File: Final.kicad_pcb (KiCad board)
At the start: 4 copper layers, 130 x 152.8 mm, 163 parts, among them J1 Power from Back_Board, J10 Conn_01x08_Socket, J11 GH-S37D, J12 LoadCell, J13 LoadCell, J14 Power to Main_Board, J15 ST-Link, J16 to TopBoard, J17 USB_C_Receptacle_USB2.0_16P, J18 LIDAR, J19 to Main_Board, J2 UnitV01, J20 to LED, J3 to LED, J4 to Tile_Board, J5 to LiDAR_Board, J6 ST-Link, J7 ST-Link, J8 UnitV02, J9 GH-S37D, M1 STS3032, M2 STS3032, M3 STS3032, M4 STS3032, SW1 RESET_SWITCH, SW10 TC-06104-043E, SW2 RESET_SWITCH, SW3 MODE_SWITCH, SW4 MODE_SWITCH, SW5 B-12CCP, SW6 B-12CCP, SW7 RESET_SWITCH, SW8 MODE_SWITCH, SW9 TC-06104-043E, U1 LT1085CM-3.3#PBF, U10 NJU77551F, U11 XIAO ESP32C3, U12 XIAO-RP2040-DIP, U13 RT9080-33GJ5, U14 CH340E, U15 STM32F446RET6, U16 AE-BNO055-BO, U17 S11059, U2 STM32F446RET6, U3 BNO085, U4 AE-BNO055-BO, U5 STM32H723ZGT6, U8 NJU77551F, U9 MAX3485

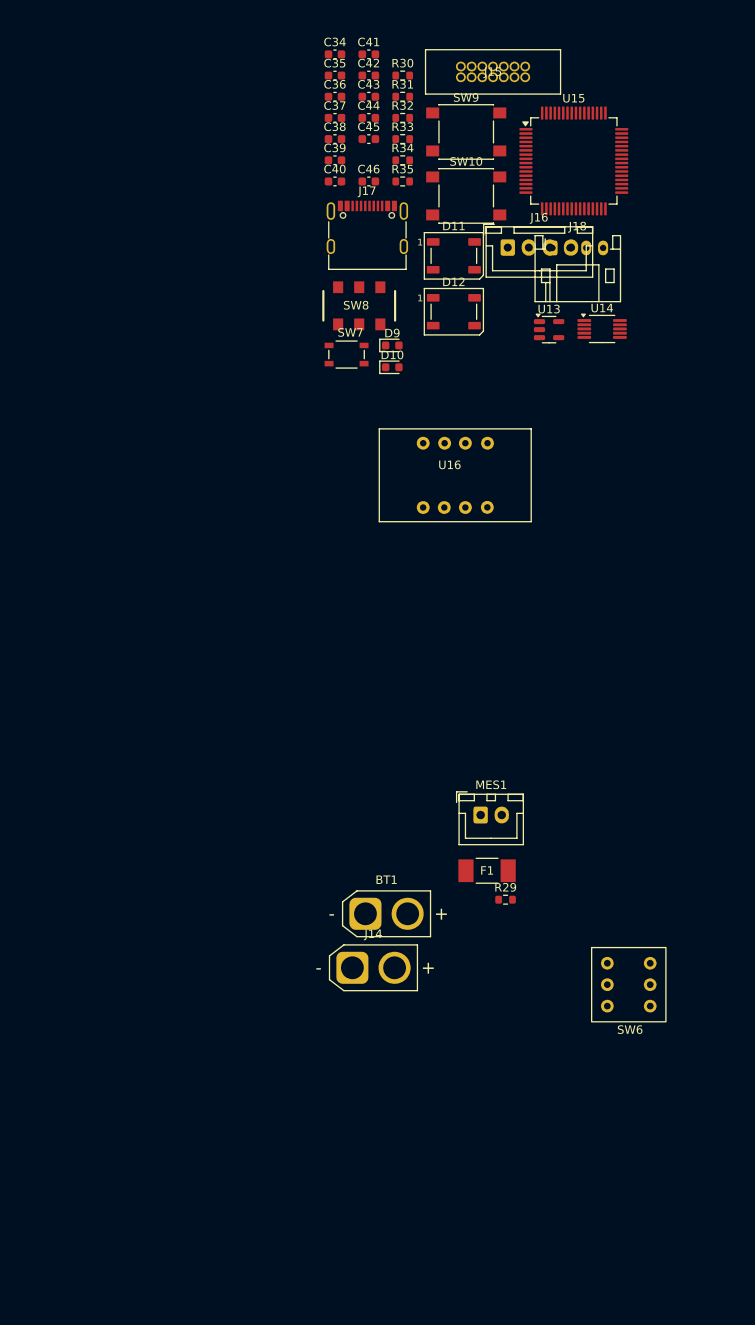
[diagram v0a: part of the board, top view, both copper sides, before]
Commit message: LiDAR基板Rev.3コネクタ配置
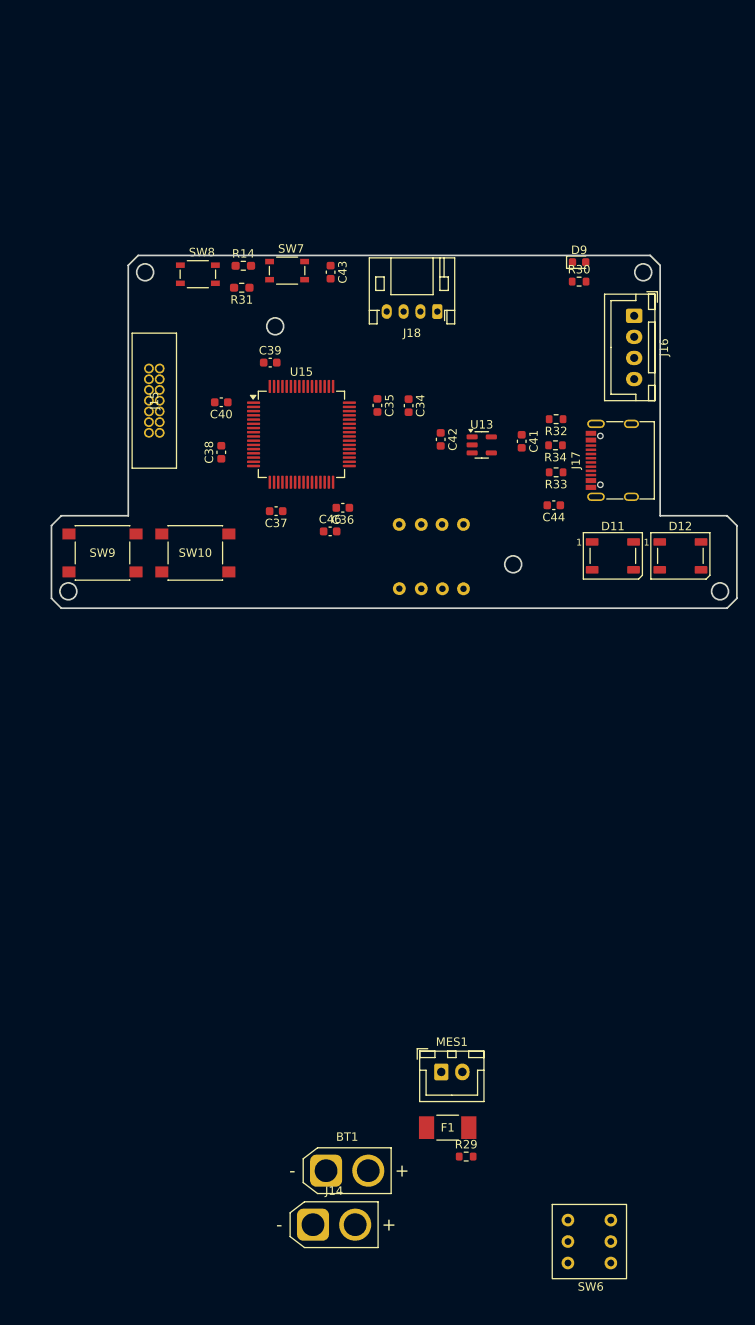
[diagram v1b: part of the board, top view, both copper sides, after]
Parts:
- removed C45: 0.1uF, Capacitor_SMD:C_0603_1608Metric
- removed D10: LED, LED_SMD:LED_0603_1608Metric
- removed R35: 470, Resistor_SMD:R_0603_1608Metric
- removed U14: CH340E, Package_SO:MSOP-10_3x3mm_P0.5mm
- added R14: 1k, Resistor_SMD:R_0603_1608Metric_Pad0.98x0.95mm_HandSolder, F.Cu at (212.8, 47.7)
- C44: value 0.1uF -> 4.7uF
- R30: value 470 -> 1k
- R31: footprint Resistor_SMD:R_0603_1608Metric -> Resistor_SMD:R_0603_1608Metric_Pad0.98x0.95mm_HandSolder
- R32: value 10k -> 1M
- R6, R8: value 10k -> 1k
- SW8: footprint SSSS213202:SSSS213202 -> SKRPACE010:SW_SKRPACE010
- U16: moved to B.Cu
- moved SW9 65.9 mm to (196.1, 81.7)
- moved J15 55.9 mm to (202.2, 63.7), turned to 90 degrees
- moved SW10 53.1 mm to (207.1, 81.7)
- moved C44 50.9 mm to (249.6, 76.0), turned to 180 degrees
- moved C41 49.3 mm to (245.8, 68.5), turned to -90 degrees
- moved C36 48.7 mm to (224.6, 76.3), turned to 180 degrees
- moved C37 47.1 mm to (216.7, 76.8), turned to 180 degrees
- moved U15 45.7 mm to (219.7, 67.7)
- moved C42 43.9 mm to (236.2, 68.2), turned to -90 degrees
- moved R33 43.5 mm to (249.8, 72.2), turned to 180 degrees
- moved C34 42.5 mm to (232.4, 64.2), turned to -90 degrees
- moved C46 41.7 mm to (223.1, 79.2)
- moved D11 40.2 mm to (256.6, 82.0)
- moved J17 40.1 mm to (257.7, 70.7), turned to 90 degrees
- moved R32 40.1 mm to (249.8, 65.8), turned to 180 degrees
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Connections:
- C44 pad 1: +5V -> Earth
- J17 pad A6: Net-(U14-UD+) -> unconnected-(J17-D+-PadA6)
- J17 pad A7: Net-(U14-UD-) -> unconnected-(J17-D--PadA7)
- J17 pad B6: Net-(U14-UD+) -> unconnected-(J17-D+-PadB6)
- J17 pad B7: Net-(U14-UD-) -> unconnected-(J17-D--PadB7)
- J17 pad S1: unconnected-(J17-SHIELD-PadS1)_2 -> Earth
- R31 pad 1: +3.3V -> GND
- R31 pad 2: Net-(SW8A-A) -> Net-(U15-BOOT0)
- R32 pad 1: GND -> Earth
- R32 pad 2: Net-(SW8A-C) -> GND
- SW8 pad 1: Net-(SW8A-A) -> Net-(R14-Pad2)
- SW8 pad 2: Net-(SW8A-B) -> Net-(U15-BOOT0)
- U15 pad 14: /LiDAR_Board/TX4 -> unconnected-(U15-PA0-Pad14)
- U15 pad 15: /LiDAR_Board/RX4 -> unconnected-(U15-PA1-Pad15)
- U15 pad 60: Net-(SW8A-B) -> Net-(U15-BOOT0)
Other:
- board size 130 x 152.8 mm -> 253.4 x 152.8 mm

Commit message: メイン基板Rev.3
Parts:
- removed BT1: Battery, Connector_AMASS:AMASS_XT30U-M_1x02_P5.0mm_Vertical
- removed F1: 0451015.MRL, 0451015.MRL:0451Series_LTF
- removed the J14 at (221.0, 161.3)
- removed MES1: Voltmeter_DC, Connector_JST:JST_XH_B2B-XH-A_1x02_P2.50mm_Vertical
- removed the R29 at (239.2, 153.2)
- removed SW10, SW9: TC-06104-043E, Button_Switch_SMD:SW_Push_1P1T_NO_6x6mm_H9.5mm
- removed SW6: B-12CCP, B-12CCP:B-12CCP
- added D12: WS2812B, LED_SMD:LED_WS2812B_PLCC4_5.0x5.0mm_P3.2mm, F.Cu at (203.7, 74.5)
- added D13: WS2812B, LED_SMD:LED_WS2812B_PLCC4_5.0x5.0mm_P3.2mm, F.Cu at (261.9, 85.3)
- added G***: LOGO, icon:jlcpcb-logo-pcb15-8, F.Cu at (243.5, 51.4)
- added G***: LOGO, icon:fornax-logo-pcb15-3.8, F.Cu at (243.6, 48.2)
- added G***: LOGO, icon:fornax-logo-pcb15-3.8, F.Cu at (232.8, 160.6)
- added IC1: R3111N211A-TR-FE, R3111N211A:SOT95P280X130-5N, F.Cu at (106.7, 47.9)
- added IC2: R3111N211A-TR-FE, R3111N211A:SOT95P280X130-5N, F.Cu at (79.2, 81.7)
- added R37: 5.6k, Resistor_SMD:R_0402_1005Metric, F.Cu at (101.2, 47.9)
- added R38: 2.4k, Resistor_SMD:R_0402_1005Metric, F.Cu at (103.5, 48.4)
- added R39: 470k, Resistor_SMD:R_0402_1005Metric, F.Cu at (106.0, 45.1)
- added R40: 5.6k, Resistor_SMD:R_0402_1005Metric, F.Cu at (74.6, 81.2)
- added R41: 470k, Resistor_SMD:R_0402_1005Metric, F.Cu at (78.5, 79.0)
- added R42: 2.4k, Resistor_SMD:R_0402_1005Metric, F.Cu at (76.1, 82.2)
- C51: renamed from C43; footprint Capacitor_SMD:C_0603_1608Metric -> Capacitor_SMD:C_0603_1608Metric_Pad1.08x0.95mm_HandSolder
- SW7, SW8: moved to B.Cu
- moved D11 62.6 mm to (203.7, 67.5)
- moved D10 58.7 mm to (207.6, 49.6)
- moved D9 39.0 mm to (251.8, 86.2), turned to 180 degrees
- moved R29 34.4 mm to (251.8, 83.9), turned to 180 degrees
- moved J16 21.6 mm to (202.6, 85.3), turned to 180 degrees
- moved J6 15.7 mm to (49.0, 37.0), turned to 90 degrees
- moved J7 15.7 mm to (116.7, 37.0), turned to -90 degrees
- moved R30 10.3 mm to (206.4, 55.7)
- moved C50 9.19 mm to (245.1, 70.3), turned to 90 degrees
- moved D7 8.48 mm to (126.1, 25.4), turned to 0 degrees
- moved C49 8.32 mm to (237.6, 70.2), turned to 90 degrees
- moved J5 7.07 mm to (112.4, 49.4)
- moved R31 5.52 mm to (211.6, 55.7)
- moved C52 5.40 mm to (254.1, 79.0)
- moved R34 4.45 mm to (254.3, 65.9)
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- renumbered C49 to C31, C48 to C32, C50 to C33, C51 to C34, C31 to C35, C32 to C36, C52 to C37, C53 to C38, C33 to C39, C54 to C40, C55 to C41, C34 to C42, C35 to C43, C36 to C44, C37 to C45, C38 to C46, C39 to C47, C40 to C48, C41 to C49, C42 to C50, C44 to C52, C46 to C53, C47 to C54, D11 to D10, D12 to D11, D13 to D14, D14 to D15, J9 to J10, J10 to J11, J11 to J12, J12 to J13, J13 to J14, J15 to J16, J16 to J17, J17 to J18, J18 to J19, J19 to J20, J20 to J9, R15 to R14, R16 to R15, R17 to R16, R18 to R17, R19 to R18, R20 to R19, R21 to R20, R22 to R21, R24 to R22, R25 to R23, R27 to R24, R28 to R25, R23 to R26, R26 to R27, R30 to R29, R14 to R30, R33 to R32, R34 to R33, R32 to R34, R36 to R35, R37 to R36, U15 to U14, U16 to U15, U17 to U16
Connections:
- D11 pad 2: unconnected-(D12-DOUT-Pad2) -> Net-(D11-DOUT)
- D2 pad 2: unconnected-(D2-DOUT-Pad2) -> Net-(D2-DOUT)
- D3 pad 4: /Main_Board/DIN1 -> Net-(D2-DOUT)
- J16 pad 8: /LiDAR_Board/SWO -> unconnected-(J16-JTDO/SWO-Pad8)
- U14 pad 33: Net-(U15-PB12) -> unconnected-(U14-PB12-Pad33)
- U14 pad 34: Net-(U15-PB13) -> unconnected-(U14-PB13-Pad34)
- U14 pad 55: /LiDAR_Board/SWO -> unconnected-(U14-PB3-Pad55)
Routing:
- net +5V: track 461.3 -> 655.7 mm, vias 3 -> 2
- net Net-(D2-DOUT): track 0.00 -> 150.4 mm, vias 0 -> 4
- net Net-(D12-DOUT): track 0.00 -> 79.6 mm, vias 0 -> 2
- net GND: track 294.5 -> 373.9 mm, vias 176 -> 236
- net /Main_Board/DIN1: track 138.6 -> 72.4 mm, vias 4 -> 2
- net /LiDAR_Board/NRST: track 0.00 -> 59.3 mm, vias 0 -> 1
- net +7.5V: track 247.9 -> 306.7 mm, vias 4 -> 8
- net /LiDAR_Board/RX3: track 0.00 -> 46.8 mm
- net +3.3V: track 174.5 -> 216.0 mm, vias 34 -> 45
- net /LiDAR_Board/TX3: track 0.00 -> 39.4 mm
- net /LiDAR_Board/SDA: track 0.00 -> 38.1 mm, vias 0 -> 1
- net /LiDAR_Board/SWCLK: track 0.00 -> 35.5 mm, vias 0 -> 1
- net /LiDAR_Board/SCL: track 0.00 -> 34.5 mm, vias 0 -> 1
- net /LiDAR_Board/SWDIO: track 0.00 -> 33.5 mm, vias 0 -> 1
- net /LiDAR_Board/RX1: track 0.00 -> 28.3 mm, vias 0 -> 1
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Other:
- outline, holes or cut-outs redrawn
- board text added: "Rev.2"

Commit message: 後ろ基板Rev.2
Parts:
- added BT1: Battery, Connector_AMASS:AMASS_XT30U-M_1x02_P5.0mm_Vertical, F.Cu at (54.4, 174.3)
- added F1: 0451015.MRL, 0451015.MRL:0451Series_LTF, F.Cu at (61.8, 167.2)
- added IC3: R3111N211A-TR-FE, R3111N211A:SOT95P280X130-5N, F.Cu at (71.5, 155.2)
- added J15: Power to Main_Board, Connector_AMASS:AMASS_XT30U-M_1x02_P5.0mm_Vertical, F.Cu at (81.2, 154.7)
- added MES1: Voltmeter_DC, Connector_JST:JST_PH_B2B-PH-K_1x02_P2.00mm_Vertical, F.Cu at (128.3, 171.1)
- added Q1: TJ15S06M3L, Package_TO_SOT_SMD:TO-252-2, F.Cu at (78.4, 169.5)
- added Q2: 2N7002, Package_TO_SOT_SMD:SOT-23, F.Cu at (97.4, 154.0)
- added Q3: 2N7002, Package_TO_SOT_SMD:SOT-23, F.Cu at (97.5, 160.0)
- added R28: 47k, Resistor_SMD:R_0603_1608Metric_Pad0.98x0.95mm_HandSolder, F.Cu at (69.7, 170.1)
- added R43: 47k, Resistor_SMD:R_0603_1608Metric_Pad0.98x0.95mm_HandSolder, F.Cu at (93.4, 153.1)
- added R44: R_Trim, 3362P-1-103LF:TRIM_3362P-1-103LF, F.Cu at (60.3, 155.4)
- added R45: 47k, Resistor_SMD:R_0603_1608Metric_Pad0.98x0.95mm_HandSolder, F.Cu at (102.2, 159.2)
- added R46: 470k, Resistor_SMD:R_0603_1608Metric_Pad0.98x0.95mm_HandSolder, F.Cu at (102.2, 153.9)
- added SW10: START_SWITCH, B12AP_NKK:B12AP_NKK, F.Cu at (127.9, 31.3)
- R13: value 1k -> 4.7k; footprint Resistor_SMD:R_0402_1005Metric -> Resistor_SMD:R_0603_1608Metric_Pad0.98x0.95mm_HandSolder
- SW5: value B-12CCP -> START_SWITCH; footprint B-12CCP:B-12CCP -> B12AP_NKK:B12AP_NKK
- moved G*** 191.5 mm to (41.8, 175.1)
- moved D14 159.9 mm to (235.9, 155.1)
- moved D15 159.9 mm to (253.9, 155.1)
- moved C54 159.9 mm to (240.6, 155.5)
- moved J20 159.9 mm to (251.2, 149.6)
- moved R35 159.9 mm to (248.1, 158.8)
- moved R36 159.9 mm to (248.1, 152.1)
- moved U16 159.9 mm to (245.8, 153.1)
- moved R13 130.6 mm to (66.6, 155.2), turned to 0 degrees
- moved SW5 124.2 mm to (107.7, 153.9)
- moved R12 4.20 mm to (126.8, 28.4)
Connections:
- R12 pad 2: Net-(R12-Pad2) -> Net-(SW10-A)
- R13 pad 1: Net-(R13-Pad1) -> Net-(MES1-+)
- R13 pad 2: Net-(U2-PB13) -> Net-(IC3-VDD)
- SW5 pad 1: Net-(R12-Pad2) -> Net-(Q3-G)
- SW5 pad 3: GND -> unconnected-(SW5-C-Pad3)
- U2 pad 33: Net-(SW5-B) -> Net-(SW10-B)
- U2 pad 34: Net-(U2-PB13) -> unconnected-(U2-PB13-Pad34)
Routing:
- net Net-(MES1-+): track 0.00 -> 126.8 mm, vias 0 -> 2
- net Net-(SW10-B): track 0.00 -> 76.1 mm, vias 0 -> 3
- net Net-(SW5-B): track 77.8 -> 5.75 mm, vias 3 -> 0
- net Net-(U2-PB13): track 68.8 -> 0.00 mm, vias 4 -> 0
- net Net-(Q1-G): track 0.00 -> 35.7 mm, vias 0 -> 2
- net Net-(IC3-OUT): track 0.00 -> 29.7 mm, vias 0 -> 2
- net Net-(BT1-+): track 0.00 -> 15.5 mm, vias 0 -> 1
- net +7.5V: track 306.7 -> 321.4 mm
- net Net-(Q3-G): track 0.00 -> 13.3 mm
- net Net-(IC3-VDD): track 0.00 -> 13.2 mm
- net Net-(Q2-S): track 0.00 -> 8.29 mm
- net /Main_Board/TX4: track 72.9 -> 64.7 mm
- net Net-(R13-Pad1): track 6.19 -> 0.00 mm
- net GND: track 373.9 -> 379.4 mm, vias 236 -> 343
- net Net-(D2-DOUT): track 150.4 -> 146.0 mm
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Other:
- board size 253.4 x 152.8 mm -> 253.6 x 159.2 mm
